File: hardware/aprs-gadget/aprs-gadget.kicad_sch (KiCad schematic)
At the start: 8 parts

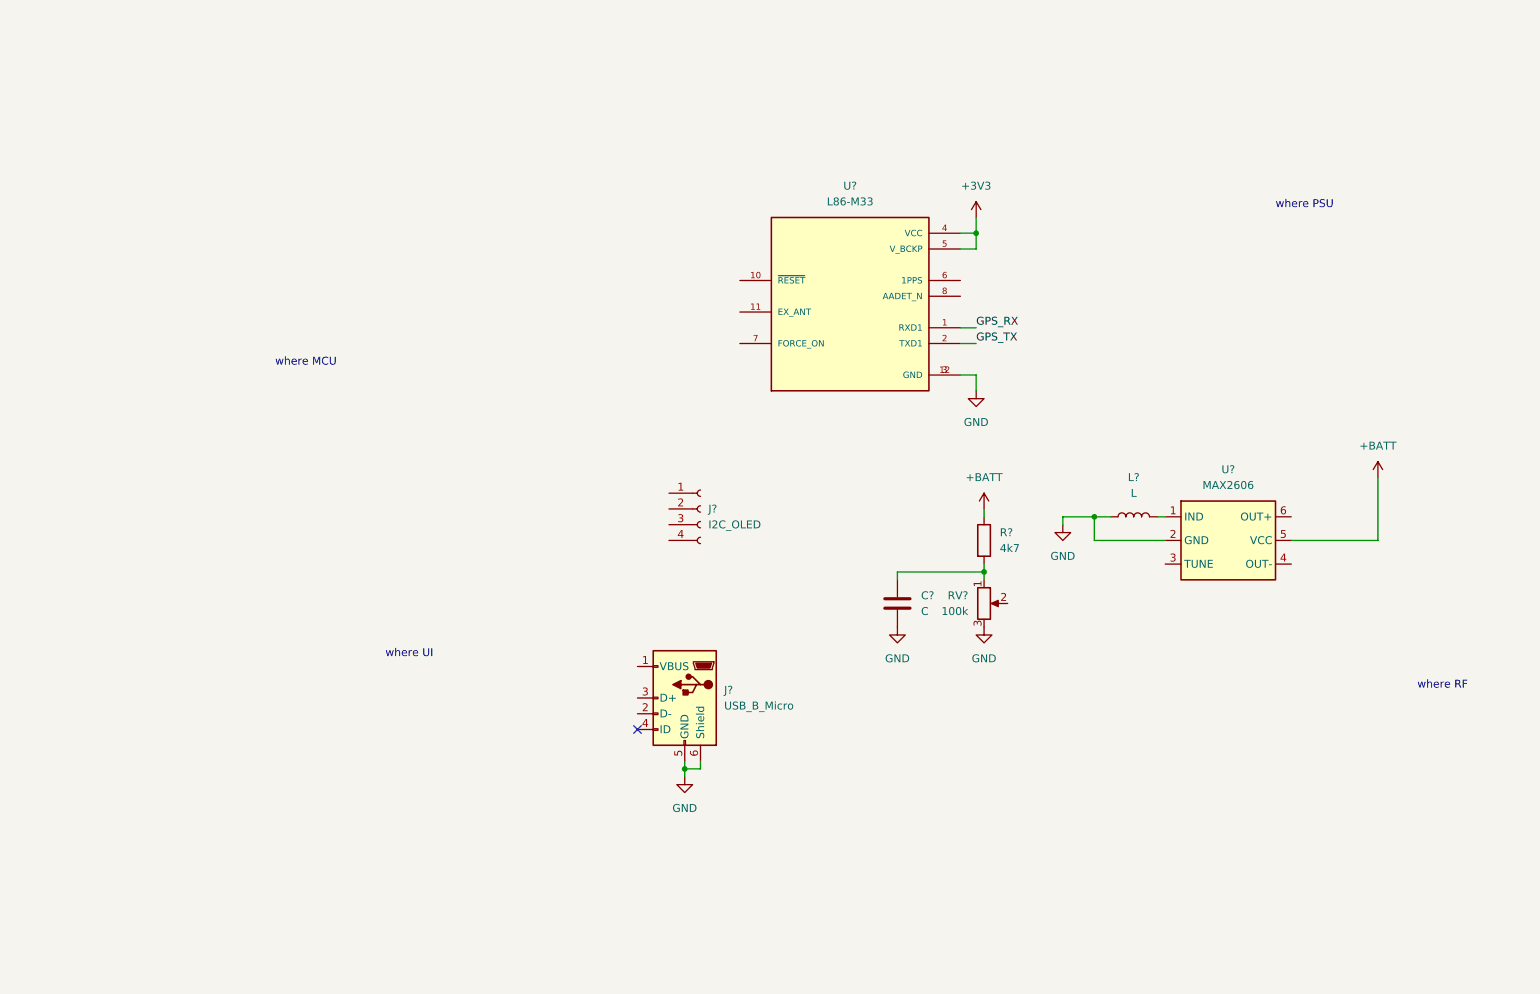
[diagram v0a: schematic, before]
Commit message: Add basic aprs firmware with fsk and packet
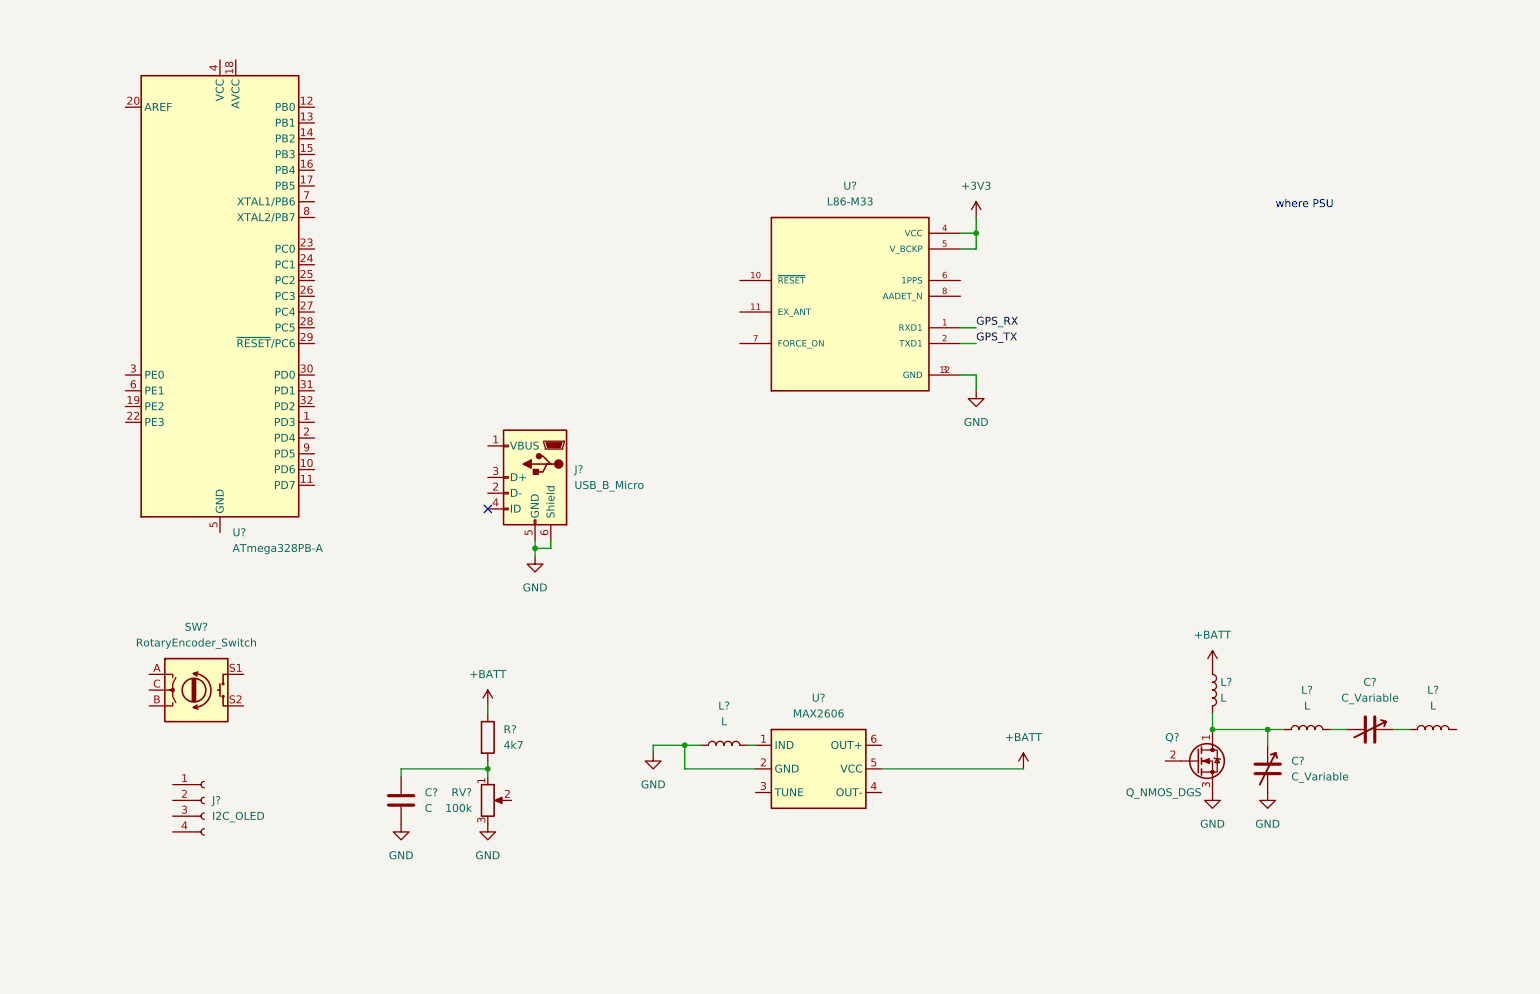
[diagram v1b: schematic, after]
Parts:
- added C? (x2): C_Variable, symbol Device:C_Variable
- added L? (x3): L, symbol Device:L
- added Q?: Q_NMOS_DGS, symbol Device:Q_NMOS_DGS
- added SW?: RotaryEncoder_Switch, symbol Device:RotaryEncoder_Switch
- added U?: ATmega328PB-A, Package_QFP:TQFP-32_7x7mm_P0.8mm, symbol MCU_Microchip_ATmega:ATmega328PB-A
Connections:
- net +BATT: now also L?.1
- net GND: now also C?.2, Q?.3 (S)
- new net: C?.1, L?.1
- new net: C?.2, L?.2
- new net: U?.21 (GND), U?.5 (GND)
- new net: C?.1, L?.1, L?.2, Q?.1 (D)
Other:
- note removed: "where MCU"
- note removed: "where RF"
- note removed: "where UI"
- moved on the sheet: C?, J?, L?, R?, RV?, U?

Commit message: Add USB bootloader
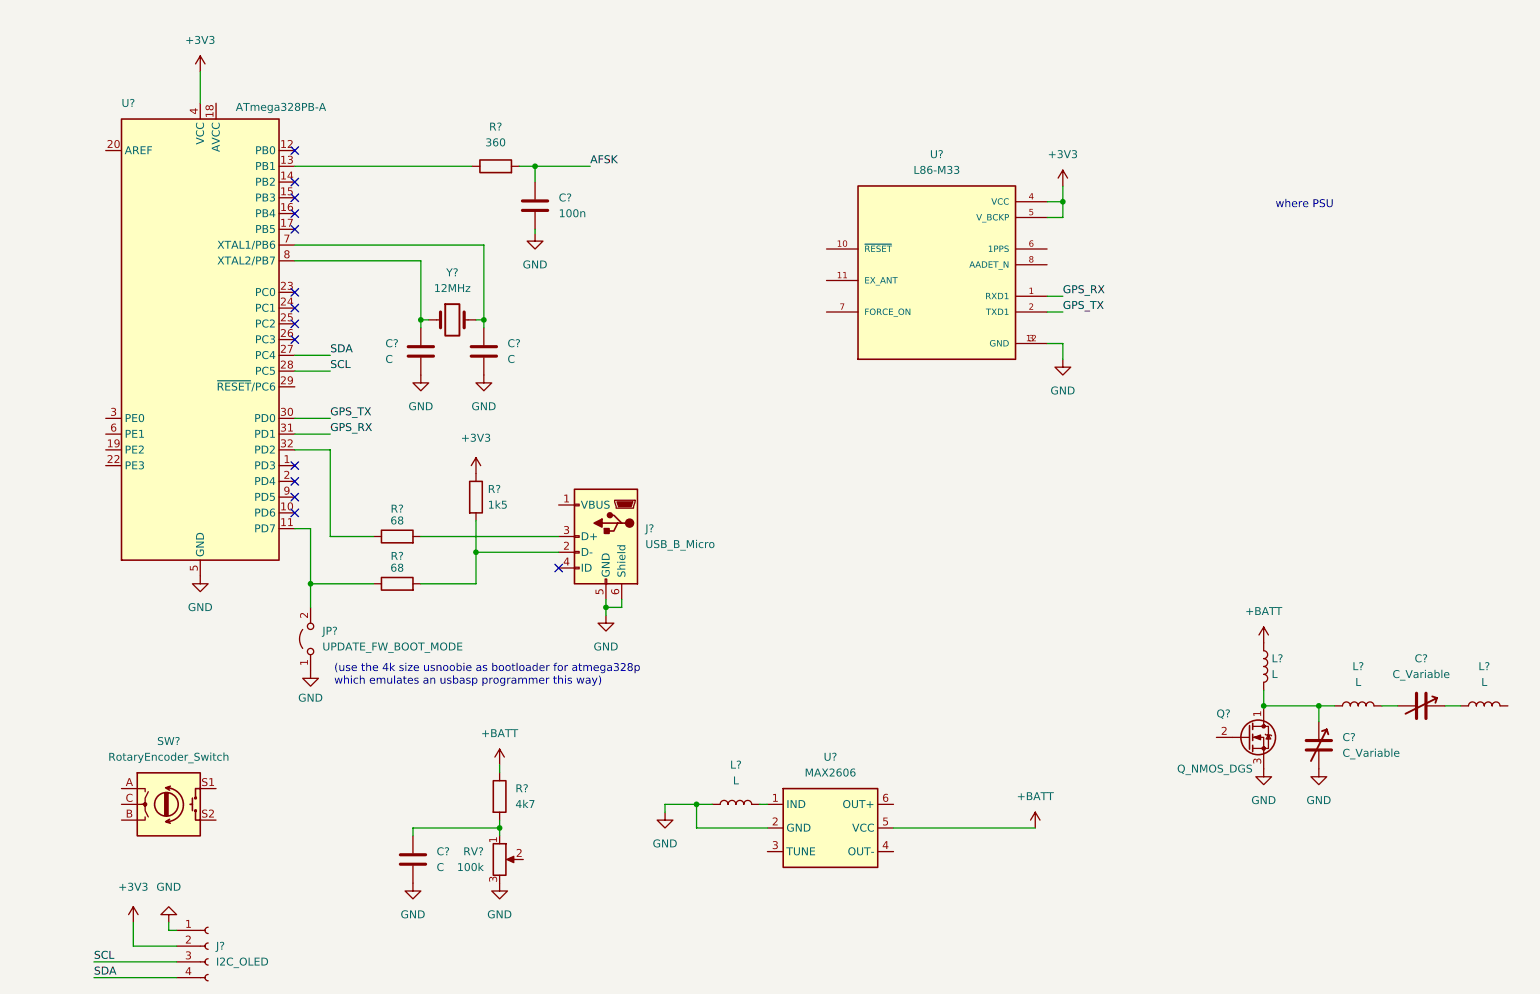
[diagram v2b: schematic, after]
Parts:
- added C? (x2): C, symbol Device:C
- added C?: 100n, symbol Device:C
- added JP?: UPDATE_FW_BOOT_MODE, symbol Jumper:Jumper_2_Open
- added R? (x2): 68, symbol Device:R
- added R?: 360, symbol Device:R
- added R?: 1k5, symbol Device:R
- added Y?: 12MHz, symbol Device:Crystal
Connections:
- net +3V3: now also J?.2 (Pin_2), U?.4 (VCC), R?.1
- net GND: now also J?.1 (Pin_1), U?.21 (GND), U?.5 (GND), C?.2, C?.2, C?.2, JP?.1 (A)
- net GPS_RX: now also U?.31 (PD1)
- net GPS_TX: now also U?.30 (PD0)
- net SCL: now reaches J?.3 (Pin_3)
- net SCL: now also U?.28 (PC5)
- net SDA: now reaches J?.4 (Pin_4)
- net SDA: now also U?.27 (PC4)
- net at J?.2 (D-): now also R?.2, R?.2
- net at J?.3 (D+): now also R?.2
- net at U?.11 (PD7): now also JP?.2 (B), R?.1
- net at U?.13 (PB1): now also R?.1
- net at U?.32 (PD2): now also R?.1
- net at U?.7 (XTAL1/PB6): now also C?.1, Y?.2
- net at U?.8 (XTAL2/PB7): now also C?.1, Y?.1
- new net AFSK: C?.1, R?.2
- no-connect marks 1 -> 14
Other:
- note added: "(use the 4k size usnoobie as bootloader for atmega328p which emulates an usbasp programmer this way)"
- moved on the sheet: C?, J?, L?, Q?, R?, RV?, SW?, U?

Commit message: Development change for STM32G030F6P6 MCU
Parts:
- removed C? (x2): C, symbol Device:C
- removed J?: USB_B_Micro, symbol Connector:USB_B_Micro
- removed JP?: UPDATE_FW_BOOT_MODE, symbol Jumper:Jumper_2_Open
- removed R? (x2): 68, symbol Device:R
- removed R?: 1k5, symbol Device:R
- removed U?: ATmega328PB-A, Package_QFP:TQFP-32_7x7mm_P0.8mm, symbol MCU_Microchip_ATmega:ATmega328PB-A
- removed Y?: 12MHz, symbol Device:Crystal
- added J?: USB_C_Receptacle_USB2.0, symbol Connector:USB_C_Receptacle_USB2.0
- added U?: STM32G030F6P6, Package_SO:TSSOP-20_4.4x6.5mm_P0.65mm, symbol STM32G030:STM32G030F6P6
- added U?: M24C16-RMN6TP, Package_SO:SOIC-8_3.9x4.9mm_P1.27mm, symbol Memory_EEPROM:AT24CS16-SSHM
- added U?: CH340E, Package_SO:MSOP-10_3x3mm_P0.5mm, symbol Interface_USB:CH340E
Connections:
- net +3V3: now also U?.4 (VDD)
- net GND: now also U?.4 (GND), U?.5 (VSS)
- net SCL: now also U?.6 (SCL)
- net SDA: now also U?.5 (SDA)
- new net: J?.A1 (GND), J?.A12 (GND), J?.B1 (GND), J?.B12 (GND)
- new net: J?.A4 (VBUS), J?.A9 (VBUS), J?.B4 (VBUS), J?.B9 (VBUS)
- new net I2C1_SCL: U?.16 (PA11[PA9])
- new net I2C1_SDA: U?.17 (PA12[PA10])
- new net SWCLK: U?.19 (PA15/PA14-BOOT0)
- new net SWDIO: U?.18 (PA13)
- new net USART1_RX: U?.1 (PB7/PB8)
- new net USART1_TX: U?.20 (PB3/PB4/PB5/PB6)
- new net USART2_RX: U?.10 (PA3)
- new net USART2_TX: U?.9 (PA2)
- no-connect marks 14 -> 0
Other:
- note removed: "(use the 4k size usnoobie as bootloader for atmega328p which emulates an usbasp programmer this way)"
- note removed: "where PSU"
- moved on the sheet: C?, R?

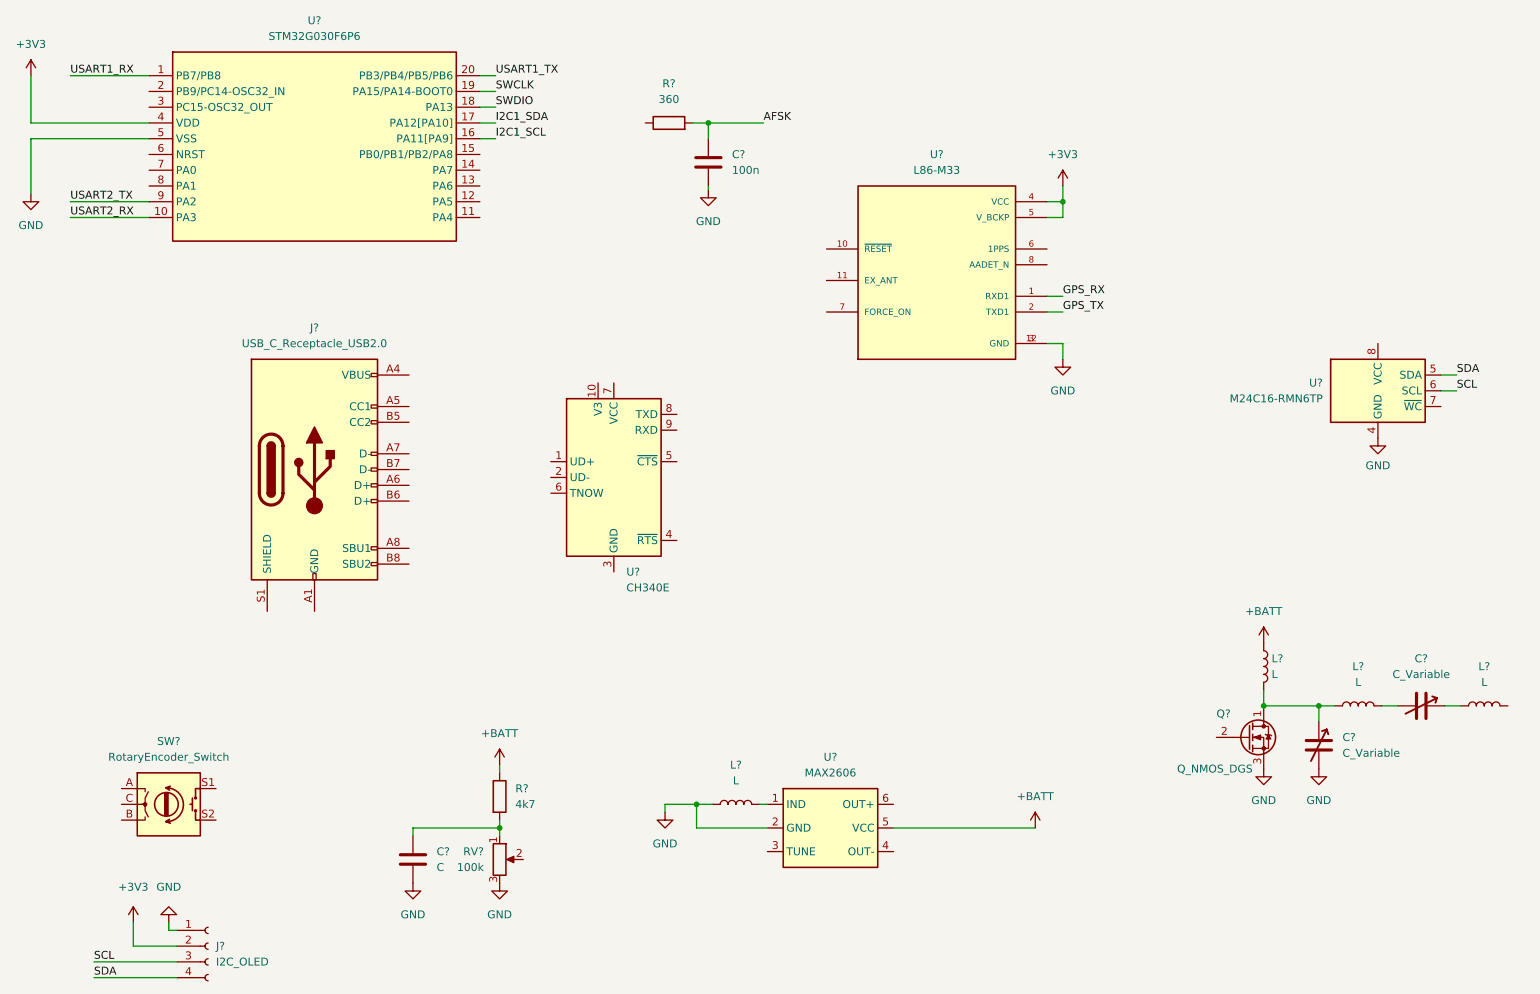
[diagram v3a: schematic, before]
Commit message: Add rotary encoder to schematic and nucleo project
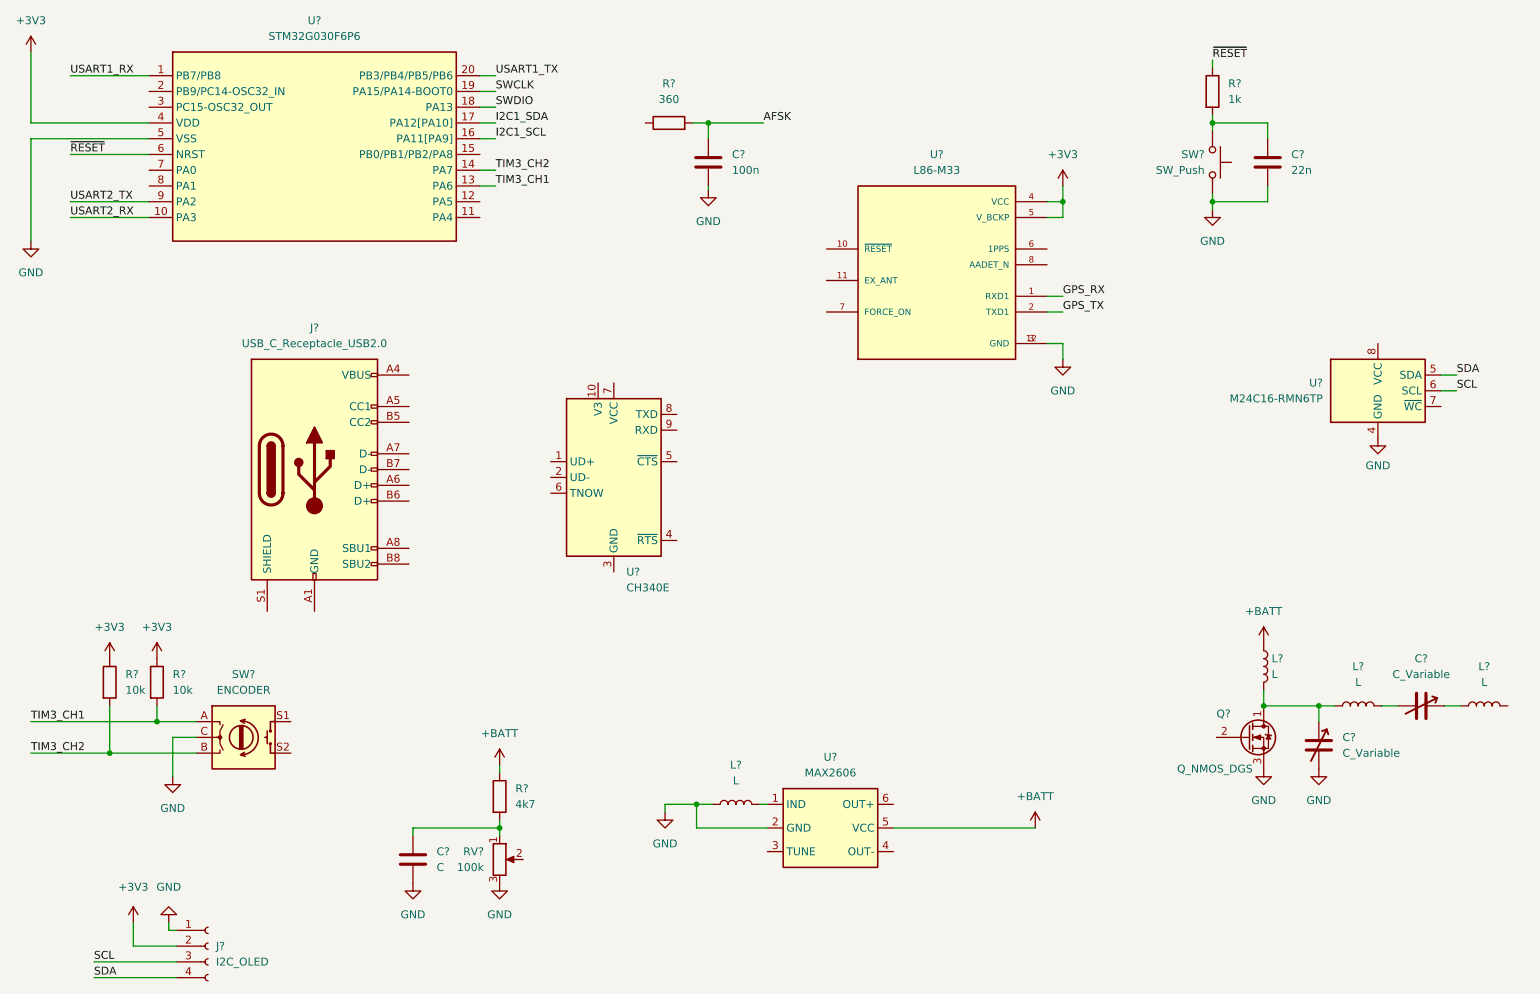
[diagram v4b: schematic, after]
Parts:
- added C?: 22n, symbol Device:C
- added R? (x2): 10k, symbol Device:R
- added R?: 1k, symbol Device:R
- added SW?: SW_Push, symbol Switch:SW_Push
- J?: footprint (none) -> Connector_USB:USB_C_Receptacle_GCT_USB4085
- SW?: value RotaryEncoder_Switch -> ENCODER
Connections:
- net +3V3: now also R?.1, R?.1
- net GND: now also SW?.C, C?.2, SW?.1
- net TIM3_CH1: now reaches U?.13 (PA6)
- net TIM3_CH1: now also SW?.A, R?.2
- net TIM3_CH2: now reaches U?.14 (PA7)
- net TIM3_CH2: now also SW?.B, R?.2
- net ~{RESET}: now reaches U?.6 (NRST)
- net ~{RESET}: now also R?.1
- new net: C?.1, R?.2, SW?.2
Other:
- moved on the sheet: SW?

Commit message: Add basic PWM generator with DMA
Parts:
- added C?: 100n, symbol Device:C
- added J?: Programming interface, symbol Connector_Generic:Conn_01x05
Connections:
- net SCL is gone; now on net I2C1_SCL: J?.3 (Pin_3), U?.6 (SCL)
- net SDA is gone; now on net I2C1_SDA: J?.4 (Pin_4), U?.5 (SDA)
- net +3V3: now also U?.8 (VCC), C?.1, J?.1 (Pin_1)
- net GND: now also C?.2, J?.3 (Pin_3)
- net SWCLK: now also J?.2 (Pin_2)
- net SWDIO: now also J?.4 (Pin_4)
- net TIM1_CH1: now reaches U?.15 (PB0/PB1/PB2/PA8)
- net TIM1_CH1: now also R?.1
- net GPS_RX: no longer names the net of U?.1 (RXD1)
- net GPS_TX: no longer names the net of U?.2 (TXD1)
- net ~{RESET} renamed NRST
- net NRST: now also J?.5 (Pin_5)
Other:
- moved on the sheet: C?, J?, R?, U?
